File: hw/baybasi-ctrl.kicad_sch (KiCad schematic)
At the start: 59 parts, among them J1 PANEL 1, J10 PANEL 10, J11 PANEL 11, J12 PANEL 12, J13 5V IN, J14 SYNC IN (opt), J2 PANEL 2, J3 PANEL 3, J4 PANEL 4, J5 PANEL 5, J6 PANEL 6, J7 PANEL 7, J8 PANEL 8, J9 PANEL 9, M1 WIZ850io J1, M2 WIZ850io J2, Q1 AO3401A, U1 SN74AHCT245N, U2 SN74AHCT245N, U3 AMS1117-3.3

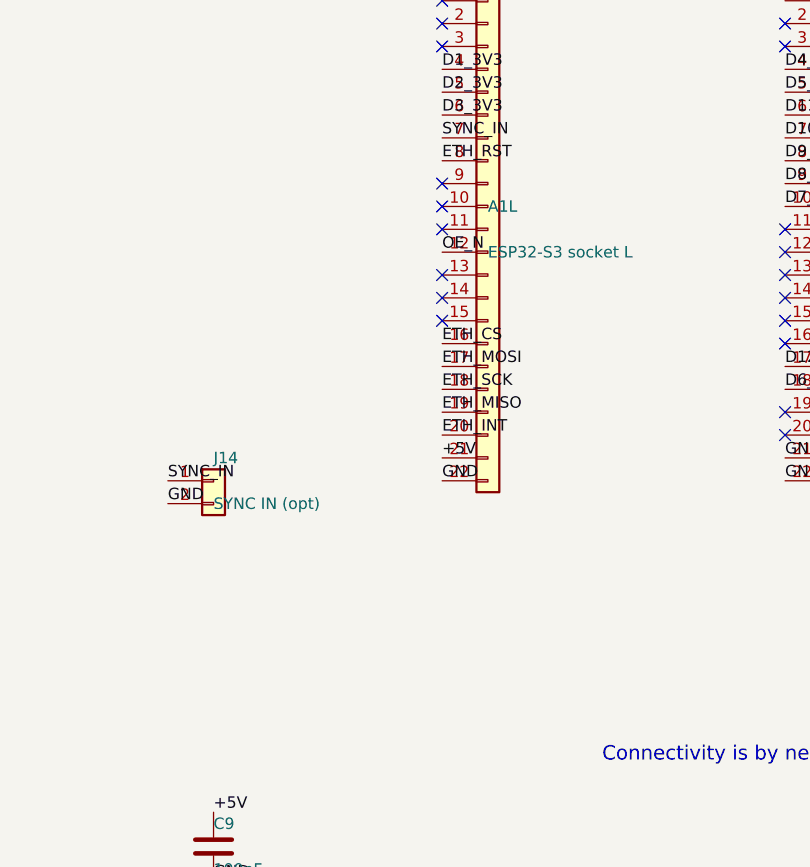
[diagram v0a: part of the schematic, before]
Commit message: hw: revB routed, DRC clean, gerbers exported
Board regenerated, routed and exported for the batch-2 run.

    0 DRC violations, 0 unconnected, 7 warnings
    all 7 are lib_footprint_mismatch - exactly batch 1's baseline

Getting there took three real fixes beyond the two intended changes:

**The right-hand cluster had to move with the socket.** A1R shifting 2.54 mm
right squeezed the A1R-to-U1 channel from ~7 mm to ~4.5 mm, and the router
could not keep the B.Cu pour continuous through it - isolated GND regions
around x 60-78, y 24-34. U1/U2 shifted +2.5 mm restores it. An earlier attempt
to paper over this with island_removal_mode made it worse (1 unconnected
region became 3) and is reverted; the channel was the cause, not the symptom.

**min_resolved_spokes is back to 1.** It went 1 -> 2 in commit 2cc4b0b, which
swept up an unvalidated working-tree change of mine and described it as "a DRC
tightening" without re-running DRC under it. It is the direct cause of 5
starved-thermal errors here (SW1 pads 7/8, A1R pad 1, J5/J8 pad 2). Batch 1
was fabricated and works at 1. Two spokes is a defensible standard but it
needs layout work, not a settings line.

**The silkscreen said revA.** Batch 2 would have shipped ten boards labelled
identically to the five already on the bench - except revA takes a 22.86 mm
devkit and revB takes 25.4 mm. Two boards that look the same, accept different
parts, and cannot be told apart without a caliper. Now split over two lines so
it clears SW1, with revB on its own line at full size.

Also adds the switch legend the spec asked for: pole weights 1 / 2 / SP / SP
beside their own poles, and COL=2+1 ON=1 below. Placing it cost three attempts
- the font runs ~0.74 mm per character at size 0.8, wider than I estimated
twice, and the board has very little free silkscreen area. The comments now
record the measured rate and say to check the placement box dump first.

CPL regenerated (U1/U2 moved, SW1 added). BOM carries SW1 / C99418.
Gerbers: baybasi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
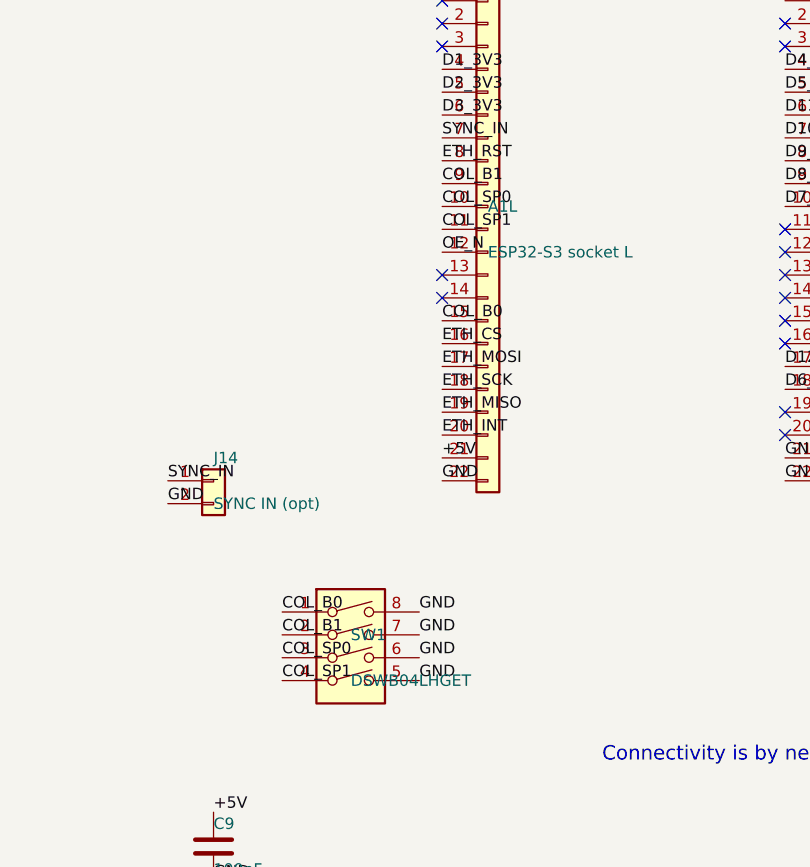
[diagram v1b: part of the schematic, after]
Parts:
- added SW1: DSWB04LHGET, Button_Switch_THT:SW_DIP_SPSTx04_Slide_9.78x12.34mm_W7.62mm_P2.54mm, symbol Switch:SW_DIP_x04
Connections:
- net GND: now also SW1.5, SW1.6, SW1.7, SW1.8
- net COL_SP0: now reaches A1L.10 (Pin_10)
- net COL_SP0: now also SW1.3
- net COL_SP1: now reaches A1L.11 (Pin_11)
- net COL_SP1: now also SW1.4
- net COL_B0: now reaches A1L.15 (Pin_15)
- net COL_B0: now also SW1.1
- net COL_B1: now reaches A1L.9 (Pin_9)
- net COL_B1: now also SW1.2
- no-connect marks 24 -> 20
